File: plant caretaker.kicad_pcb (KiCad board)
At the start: 2 copper layers, 60.5 x 98.5 mm, 56 parts, among them J3 Water_Pump, J4 Kitronik, J5 694106402002, Q1 FDMS86255, U1 UDA1380HN_N2, U2 TMP175AIDR, U4 LM2596S-5, U5 PAM8403D, U6 ESP32_C3_ZERO

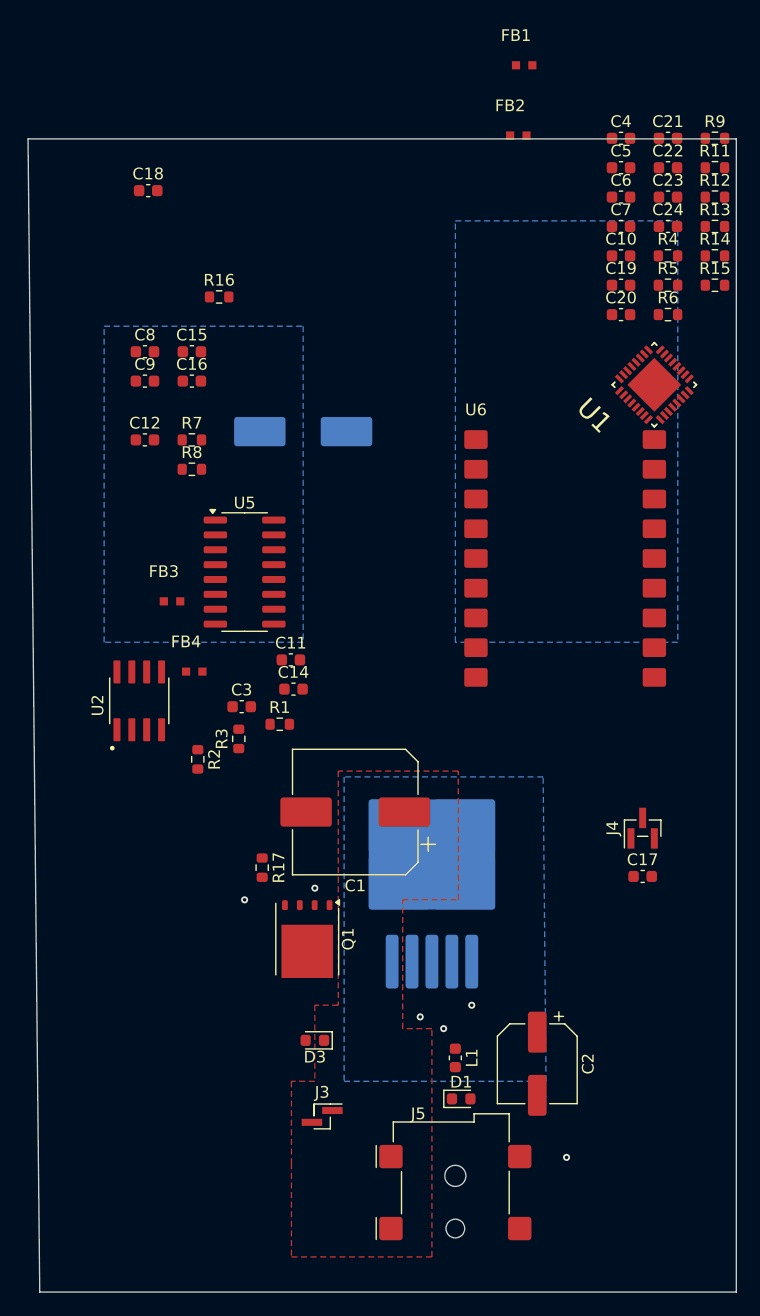
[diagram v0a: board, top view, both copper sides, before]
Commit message: Began connecting digital connections
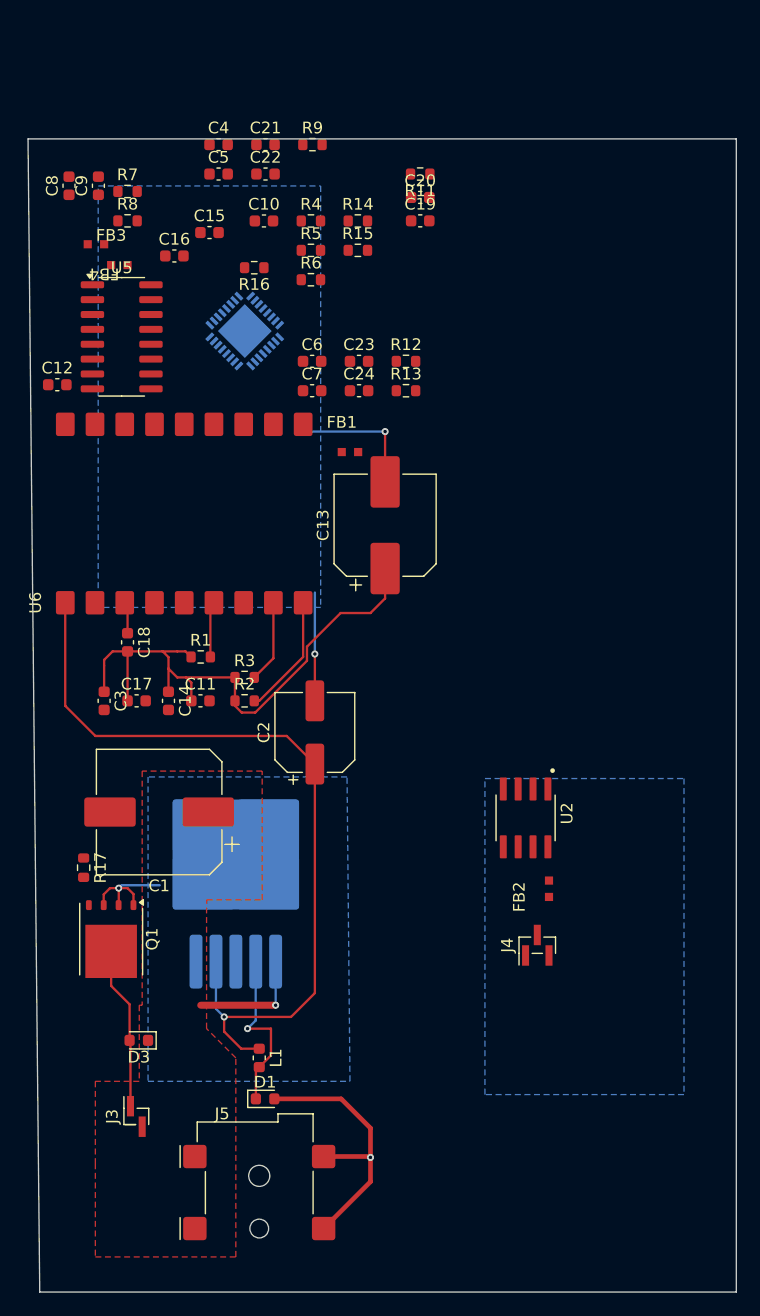
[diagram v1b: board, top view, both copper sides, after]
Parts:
- C13: moved to F.Cu
- U1: moved to B.Cu
- moved FB2 65.1 mm to (126.0, 107.8), turned to 90 degrees
- moved C17 45.8 mm to (90.8, 91.0)
- moved C18 38.6 mm to (90.0, 86.0), turned to -90 degrees
- moved U6 37.7 mm to (84.7, 82.6), turned to 90 degrees
- moved FB4 37.2 mm to (88.0, 52.0), turned to 180 degrees
- moved FB1 36.2 mm to (108.3, 69.8)
- moved U1 35.3 mm to (100.0, 59.4), turned to 45 degrees
- moved U2 34.5 mm to (124.0, 101.0), turned to -90 degrees
- moved R9 34.4 mm to (105.8, 43.5)
- moved C21 34.4 mm to (101.8, 43.5)
- moved C22 34.4 mm to (101.8, 46.0)
- moved C4 34.4 mm to (97.8, 43.5)
- moved C5 34.4 mm to (97.8, 46.0)
- moved C2 34.1 mm to (106.0, 93.7), turned to 90 degrees
- moved R14 30.6 mm to (109.7, 50.0)
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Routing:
- net /BuckConverter/5V_OUT: track 0.00 -> 70.2 mm
- net GND: track 0.13 -> 53.2 mm, vias 3 -> 4
- net +3V3: track 0.00 -> 49.5 mm
- net Net-(D1-K): track 0.00 -> 14.5 mm
- net Net-(D3-A): track 0.00 -> 13.9 mm
- net /AudioCodec/SCL: track 0.00 -> 10.4 mm
- net /BuckConverter/12V: track 0.04 -> 10.2 mm
- net /AudioCodec/SDA: track 0.00 -> 7.06 mm
- net /TempSensor/ALERT: track 0.00 -> 4.76 mm
- net Net-(U6-3V3_OUT): track 0.00 -> 2.70 mm

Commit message: Trying different layout for digital part
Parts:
- moved FB2 49.5 mm to (126.5, 58.3), turned to -90 degrees
- moved J4 40.7 mm to (125.5, 71.1), turned to 180 degrees
- moved U2 37.5 mm to (124.0, 63.5), turned to 0 degrees
- moved FB1 35.4 mm to (73.0, 73.5)
- moved FB4 35.0 mm to (60.0, 73.0)
- moved R7 33.4 mm to (101.0, 79.0), turned to 180 degrees
- moved R8 30.3 mm to (86.0, 80.0)
- moved C15 27.8 mm to (74.2, 67.0)
- moved C9 27.7 mm to (103.0, 70.0)
- moved R16 27.0 mm to (75.0, 62.0)
- moved C16 25.1 mm to (104.0, 76.0)
- moved C8 22.1 mm to (87.0, 69.0)
- moved R12 20.8 mm to (108.2, 42.0), turned to 180 degrees
- moved U6 19.0 mm to (84.6, 63.6)
- moved FB3 18.2 mm to (88.0, 72.0), turned to 180 degrees
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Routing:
- net GND: track 53.2 -> 81.4 mm, vias 4 -> 5
- net +3V3: track 49.5 -> 67.0 mm
- net /BuckConverter/PWM_IN: track 0.00 -> 3.67 mm
- net Net-(Q1-G): track 0.00 -> 2.56 mm

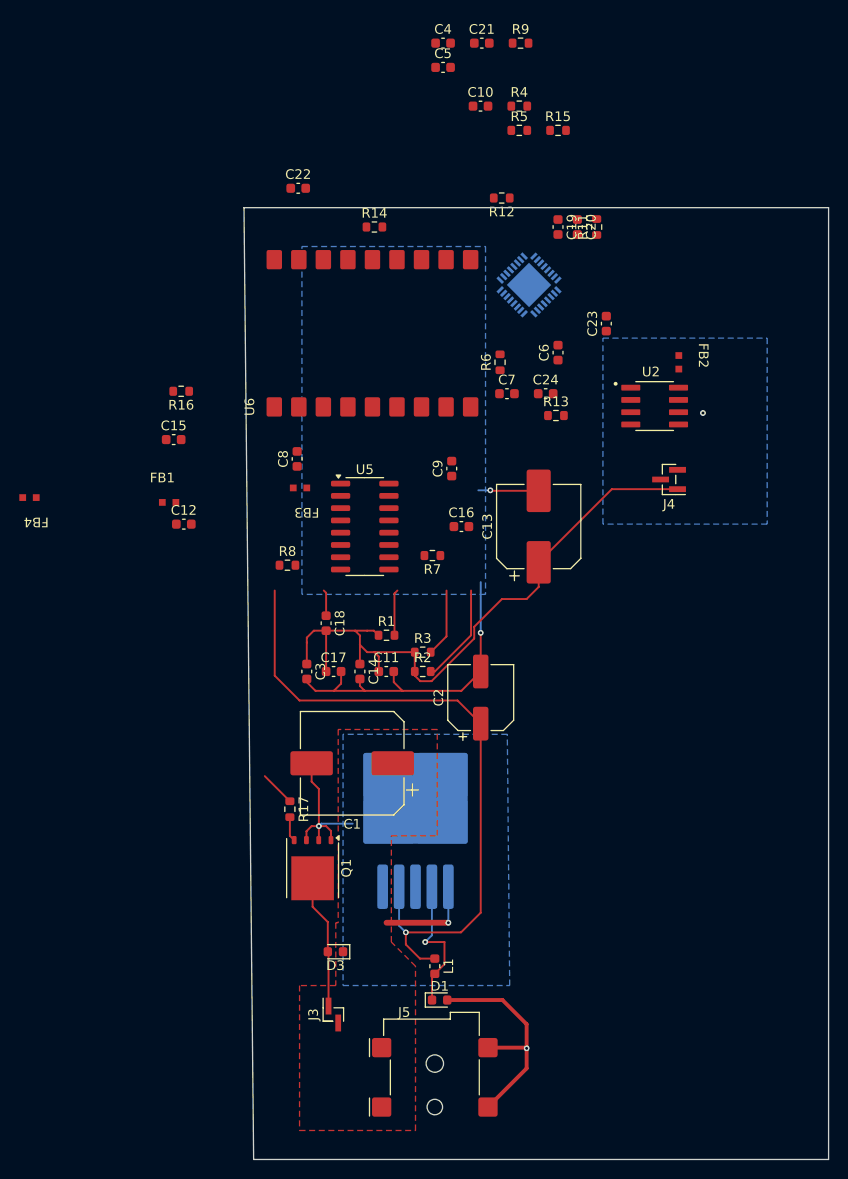
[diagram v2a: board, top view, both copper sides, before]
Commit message: Connected more components
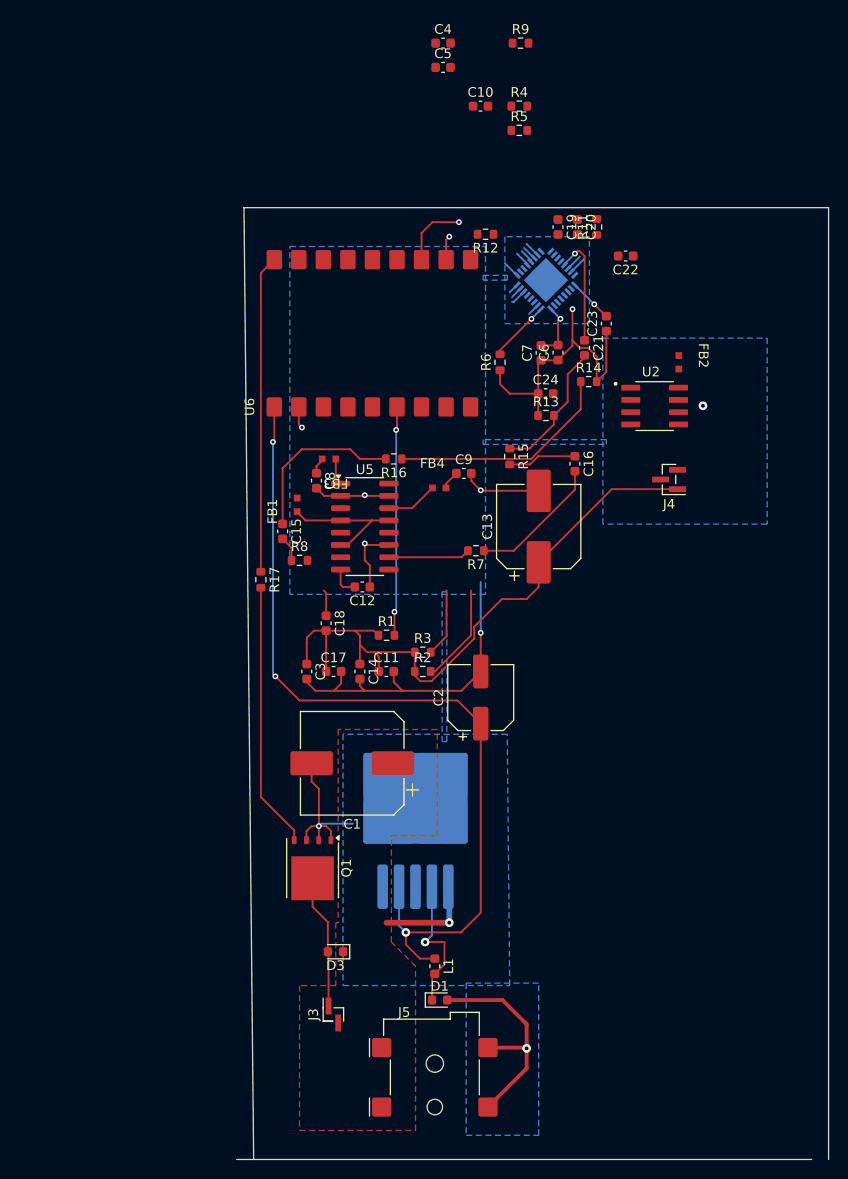
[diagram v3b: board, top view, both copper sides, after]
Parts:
- moved FB4 41.0 mm to (101.0, 72.0), turned to 0 degrees
- moved C22 34.6 mm to (121.0, 48.0), turned to 180 degrees
- moved R15 34.1 mm to (109.0, 68.8), turned to -90 degrees
- moved C21 33.3 mm to (116.8, 57.5), turned to -90 degrees
- moved R14 27.3 mm to (117.2, 61.0)
- moved R17 23.9 mm to (83.2, 81.5)
- moved R16 23.1 mm to (97.0, 69.0)
- moved C12 19.6 mm to (93.8, 82.2), turned to 180 degrees
- moved C15 14.7 mm to (85.5, 76.5), turned to -90 degrees
- moved FB1 14.0 mm to (87.0, 74.5), turned to 90 degrees
- moved C16 13.4 mm to (115.8, 69.5), turned to -90 degrees
- moved C7 5.51 mm to (112.2, 58.0), turned to 90 degrees
- moved R7 4.53 mm to (105.5, 78.5)
- moved FB3 4.24 mm to (91.0, 69.0)
- moved R12 4.11 mm to (106.5, 45.8)
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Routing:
- net GND: track 81.4 -> 131.5 mm, vias 5 -> 9
- net /BuckConverter/PWM_IN: track 3.67 -> 32.9 mm
- net Net-(Q1-G): track 2.56 -> 27.6 mm
- net Net-(C22-Pad1): track 0.00 -> 23.5 mm
- net /BuckConverter/5V_OUT: track 70.2 -> 89.4 mm, vias 1 -> 3
- net /TempSensor/ALERT: track 4.76 -> 23.7 mm, vias 0 -> 2
- net /AudioAmplifier/L_IN: track 0.00 -> 17.7 mm
- net +3V3: track 67.0 -> 81.2 mm
- net Net-(C21-Pad2): track 0.00 -> 14.1 mm
- net Net-(C16-Pad2): track 0.00 -> 13.9 mm
- net Net-(U1-VOUTR): track 0.00 -> 11.7 mm, vias 0 -> 1
- net Net-(U5-INR): track 0.00 -> 8.45 mm
- net /CODEC.WSI: track 0.00 -> 8.35 mm, vias 0 -> 1
- net /AudioAmplifier/R_IN: track 0.00 -> 7.10 mm
- net Net-(U1-RESET): track 0.00 -> 6.45 mm, vias 0 -> 1
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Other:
- board size 60.5 x 98.5 mm -> 61.2 x 98.5 mm

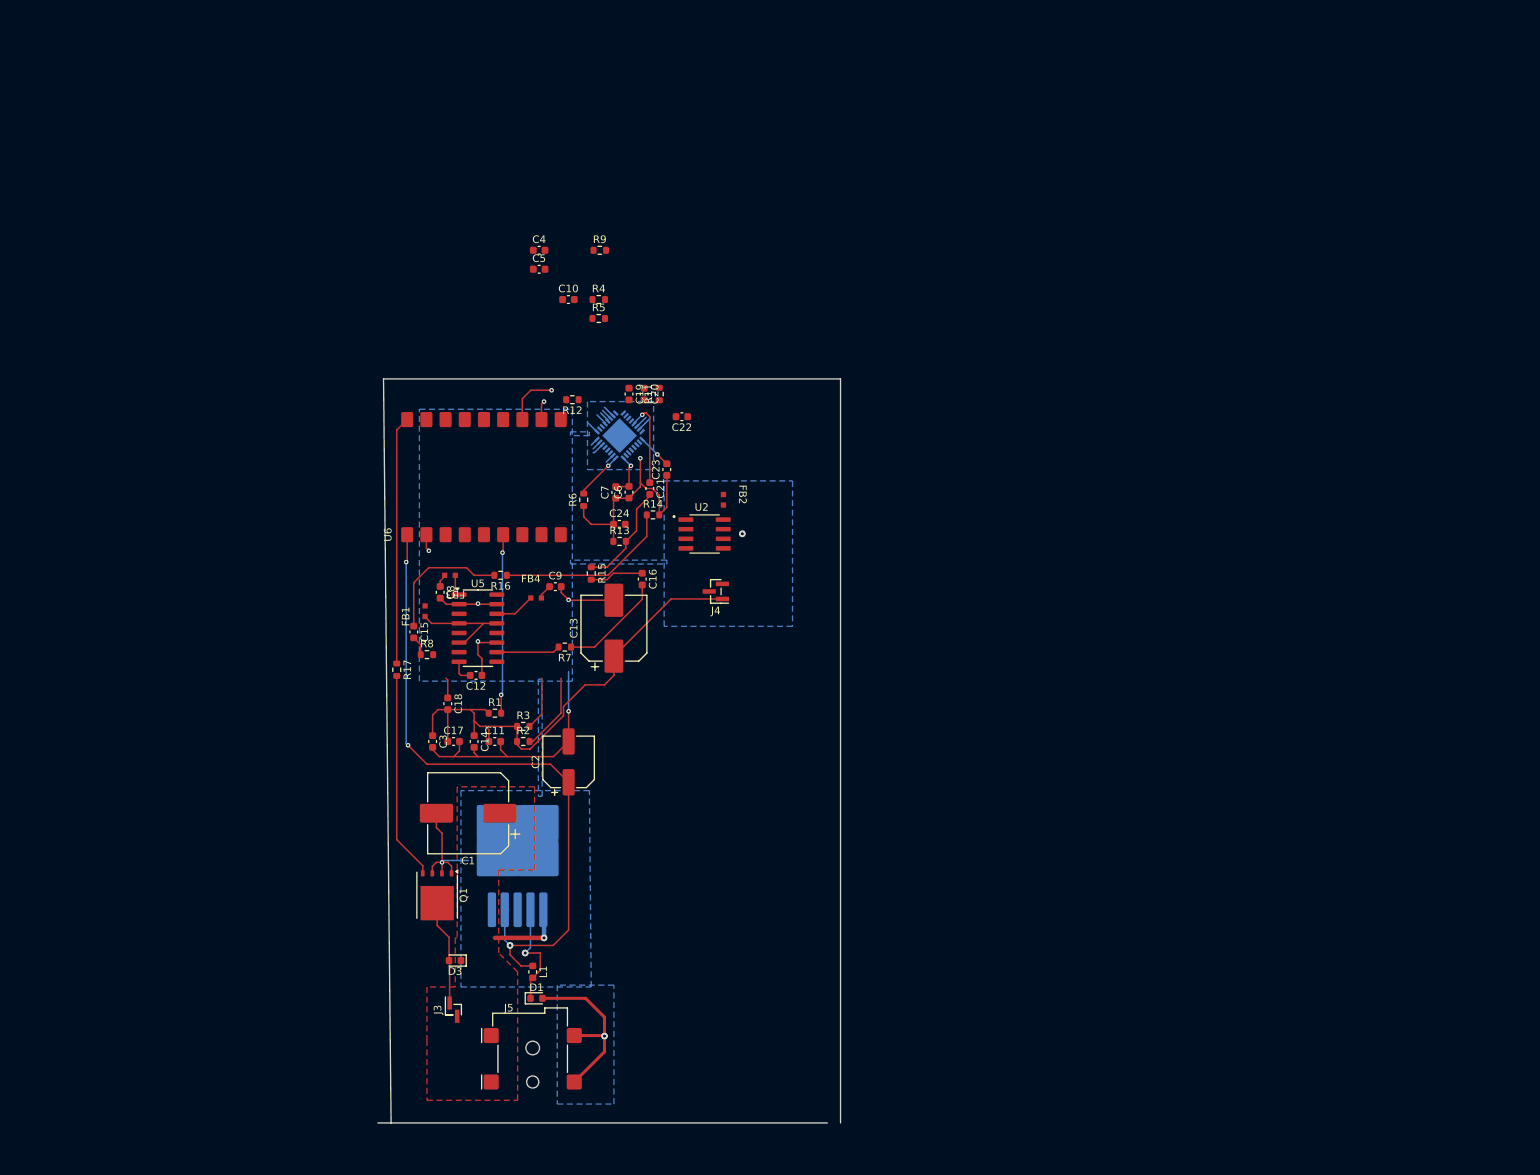
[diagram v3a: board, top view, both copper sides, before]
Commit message: Made more connections
And re-imported ferrite beads footprints
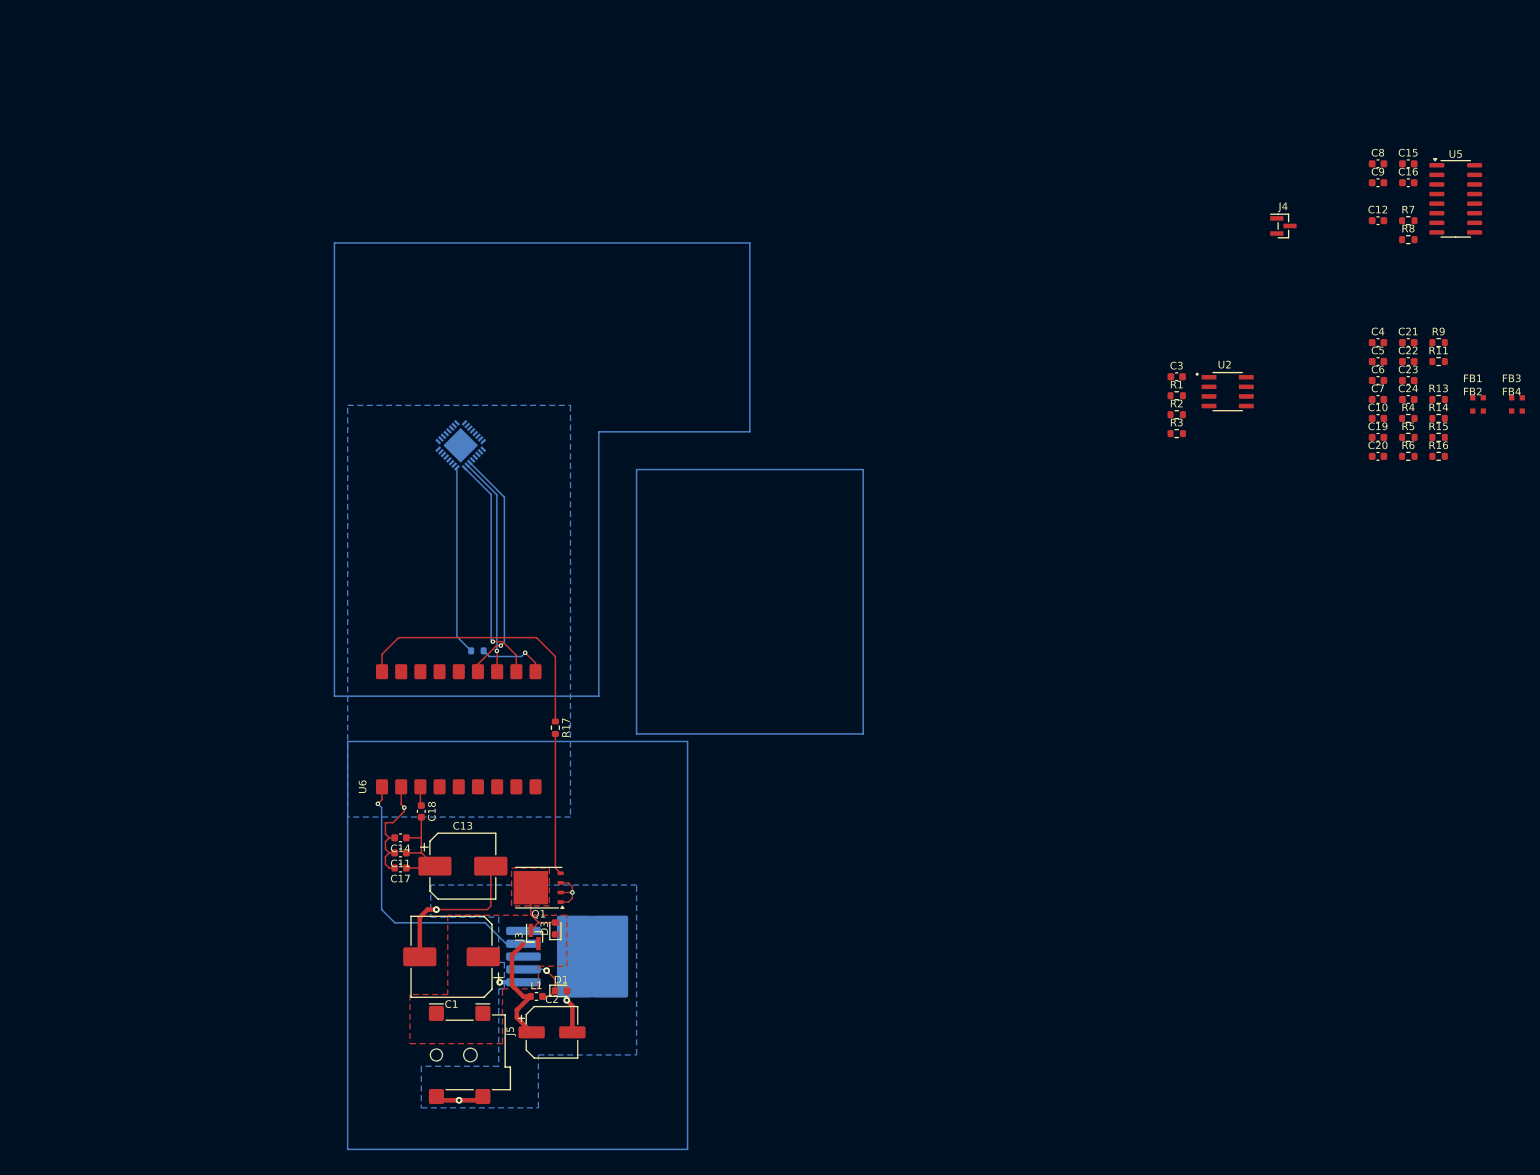
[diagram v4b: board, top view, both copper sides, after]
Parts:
- R12: moved to B.Cu
- moved C15 145.5 mm to (217.2, 14.5), turned to 0 degrees
- moved FB3 141.8 mm to (230.8, 45.5), turned to 0 degrees
- moved FB1 141.7 mm to (225.7, 45.5), turned to 0 degrees
- moved U5 141.4 mm to (223.4, 19.2)
- moved R8 141.1 mm to (217.2, 24.6)
- moved C8 136.5 mm to (213.2, 14.5), turned to 0 degrees
- moved C12 133.7 mm to (213.2, 22.1), turned to 0 degrees
- moved FB4 132.2 mm to (230.8, 47.2)
- moved R16 125.2 mm to (221.2, 53.2), turned to 0 degrees
- moved R7 125.1 mm to (217.2, 22.1), turned to 0 degrees
- moved C9 121.3 mm to (213.2, 17.0)
- moved C16 114.2 mm to (217.2, 17.0), turned to 0 degrees
- moved R15 113.6 mm to (221.2, 50.7), turned to 0 degrees
- moved R9 111.7 mm to (221.2, 38.2)
- moved C4 111.7 mm to (213.2, 38.2)
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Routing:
- net GND: track 131.5 -> 55.3 mm, vias 9 -> 5
- net +3V3: track 81.2 -> 15.1 mm
- net /BuckConverter/5V_OUT: track 89.4 -> 52.9 mm, vias 3 -> 1
- net /CODEC.BCKI: track 1.65 -> 31.4 mm, vias 0 -> 1
- net /CODEC.DATAI: track 3.60 -> 30.6 mm
- net /TempSensor/ALERT: track 23.7 -> 0.00 mm, vias 2 -> 0
- net Net-(C22-Pad1): track 23.5 -> 0.00 mm
- net Net-(U1-SYSCLK): track 1.79 -> 25.0 mm
- net /CODEC.WSI: track 8.35 -> 29.0 mm
- net /AudioAmplifier/L_IN: track 17.7 -> 0.00 mm
- net Net-(C21-Pad2): track 14.1 -> 0.00 mm
- net Net-(C16-Pad2): track 13.9 -> 0.00 mm
- net /AudioCodec/SCL: track 11.8 -> 0.00 mm
- net Net-(U1-VOUTR): track 11.7 -> 0.00 mm, vias 1 -> 0
- net /CODEC.SYSCLK: track 0.00 -> 9.10 mm, vias 0 -> 1
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- added copper zone on F.Cu, net Net-(D3-A)
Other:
- board outline removed
